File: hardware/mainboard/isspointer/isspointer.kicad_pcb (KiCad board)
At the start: 2 copper layers, 33 parts, among them J1 USB_B_Micro, Q1 SS8050-G, Q2 SS8050-G, SW1 SW_Push, SW2 SW_Push, U1 AMS1117-3.3, U2 CP2102N-A01-GQFN28, U3 esp32-WROOM-32D, U4 DRV8834_HTSSOP

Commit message: stepper drivers
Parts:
- added C10: 10nF/50V(10%), Capacitor_SMD:C_0603_1608Metric_Pad1.05x0.95mm_HandSolder, F.Cu at (102.2, 64.1)
- added C11: 4.7uF/6.3V(10%), Capacitor_SMD:C_0603_1608Metric_Pad1.05x0.95mm_HandSolder, F.Cu at (110.2, 61.6)
- added C12: 100 uF 16V, Capacitor_SMD:CP_Elec_6.3x4.9, F.Cu at (106.0, 71.1)
- added C13: 10uF/10V(20%), Capacitor_SMD:C_0603_1608Metric_Pad1.05x0.95mm_HandSolder, F.Cu at (118.7, 64.1)
- added C14: 0.1uF/50V(10%), Capacitor_SMD:C_0603_1608Metric_Pad1.05x0.95mm_HandSolder, F.Cu at (118.7, 67.3)
- added C15: 0.1uF/50V(10%), Capacitor_SMD:C_0603_1608Metric_Pad1.05x0.95mm_HandSolder, F.Cu at (118.7, 70.5)
- added C16: 10uF/10V(20%), Capacitor_SMD:C_0603_1608Metric_Pad1.05x0.95mm_HandSolder, F.Cu at (118.7, 74.3)
- added C17: 10nF/50V(10%), Capacitor_SMD:C_0603_1608Metric_Pad1.05x0.95mm_HandSolder, F.Cu at (131.4, 61.0)
- added C18: 4.7uF/6.3V(10%), Capacitor_SMD:C_0603_1608Metric_Pad1.05x0.95mm_HandSolder, F.Cu at (127.0, 63.5)
- added C19: 100 uF 16V, Capacitor_SMD:CP_Elec_6.3x4.9, F.Cu at (130.2, 70.5)
- added C20: 10uF/10V(20%), Capacitor_SMD:C_0603_1608Metric_Pad1.05x0.95mm_HandSolder, F.Cu at (141.0, 61.0)
- added C21: 0.1uF/50V(10%), Capacitor_SMD:C_0603_1608Metric_Pad1.05x0.95mm_HandSolder, F.Cu at (140.7, 65.4)
- added C22: 0.1uF/50V(10%), Capacitor_SMD:C_0603_1608Metric_Pad1.05x0.95mm_HandSolder, F.Cu at (141.0, 67.9)
- added C23: 10uF/10V(20%), Capacitor_SMD:C_0603_1608Metric_Pad1.05x0.95mm_HandSolder, F.Cu at (141.0, 71.8)
- added J2: Motor 1, Connector_JST:JST_XH_B5B-XH-A_1x05_P2.50mm_Vertical, F.Cu at (112.2, 35.6)
- added J3: Motor 2, Connector_JST:JST_XH_B5B-XH-A_1x05_P2.50mm_Vertical, F.Cu at (137.7, 34.9)
- added R11: 47K(5%), Resistor_SMD:R_0603_1608Metric_Pad1.05x0.95mm_HandSolder, F.Cu at (107.3, 48.9)
- added R12: 1.5K(5%), Resistor_SMD:R_0603_1608Metric_Pad1.05x0.95mm_HandSolder, F.Cu at (115.0, 69.6)
- added R13: 10K(5%), Resistor_SMD:R_0603_1608Metric_Pad1.05x0.95mm_HandSolder, F.Cu at (112.4, 68.6)
- added R14: 47K(5%), Resistor_SMD:R_0603_1608Metric_Pad1.05x0.95mm_HandSolder, F.Cu at (115.2, 50.2)
- added R15: 47K(5%), Resistor_SMD:R_0603_1608Metric_Pad1.05x0.95mm_HandSolder, F.Cu at (115.6, 54.6)
- added R16: 100(5%) 1W, Resistor_SMD:R_2512_6332Metric_Pad1.52x3.35mm_HandSolder, F.Cu at (101.6, 44.5)
- added R17: 100(5%) 1W, Resistor_SMD:R_2512_6332Metric_Pad1.52x3.35mm_HandSolder, F.Cu at (113.7, 44.5)
- added R18: 1(20%), Resistor_SMD:R_0603_1608Metric_Pad1.05x0.95mm_HandSolder, F.Cu at (115.0, 72.1)
- added R19: 47K(5%), Resistor_SMD:R_0603_1608Metric_Pad1.05x0.95mm_HandSolder, F.Cu at (132.1, 48.3)
- added R20: 1.5K(5%), Resistor_SMD:R_0603_1608Metric_Pad1.05x0.95mm_HandSolder, F.Cu at (132.5, 65.4)
- added R21: 10K(5%), Resistor_SMD:R_0603_1608Metric_Pad1.05x0.95mm_HandSolder, F.Cu at (135.9, 67.9)
- added R22: 47K(5%), Resistor_SMD:R_0603_1608Metric_Pad1.05x0.95mm_HandSolder, F.Cu at (139.1, 49.5)
- added R23: 47K(5%), Resistor_SMD:R_0603_1608Metric_Pad1.05x0.95mm_HandSolder, F.Cu at (139.1, 54.0)
- added R24: 100(5%) 1W, Resistor_SMD:R_2512_6332Metric_Pad1.52x3.35mm_HandSolder, F.Cu at (127.0, 43.8)
- added R25: 100(5%) 1W, Resistor_SMD:R_2512_6332Metric_Pad1.52x3.35mm_HandSolder, F.Cu at (138.4, 43.8)
- added R26: 1(20%), Resistor_SMD:R_0603_1608Metric_Pad1.05x0.95mm_HandSolder, F.Cu at (138.4, 76.8)
- added RV1: R_POT_US, digikey-footprints:Trimpot_3.8mmx3.6mm_TC33X-2-103E, F.Cu at (116.2, 58.4)
- added RV2: R_POT_US, digikey-footprints:Trimpot_3.8mmx3.6mm_TC33X-2-103E, F.Cu at (140.3, 57.8)
- added U5: DRV8834_HTSSOP, isspointer:DRV8834PWPR, F.Cu at (131.4, 55.2)
- moved U4 16.8 mm to (107.3, 55.9), turned to 270 degrees
- moved SW1 2.54 mm to (92.7, 62.2)
- moved C8 1.79 mm to (83.6, 65.5)
- moved C7 1.27 mm to (83.4, 59.4)
- moved C9 1.27 mm to (83.3, 62.7)
- moved SW2 1.27 mm to (73.7, 62.2)
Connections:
- net Net-(U4-Pad11) renamed /STEP_1
- net Net-(U4-Pad12) renamed /DIR_1
- net VDD renamed +3V3
- U4 pad 1: Net-(U4-Pad1) -> /ENABLE_1
- U4 pad 13: Net-(U4-Pad13) -> GNDREF
- U4 pad 14: Net-(U4-Pad14) -> GNDREF
- U4 pad 18: Net-(U4-Pad18) -> VBUS
- U4 pad 19: Net-(U4-Pad19) -> VBUS
- U4 pad 20: Net-(U4-Pad20) -> +5V
- U4 pad 21: Net-(U4-Pad21) -> Net-(RV1-Pad3)
- U4 pad 22: Net-(U4-Pad22) -> Net-(RV1-Pad2)
- U4 pad 23: Net-(U4-Pad23) -> Net-(RV1-Pad2)
- U4 pad 25: Net-(U4-Pad25) -> Net-(RV1-Pad3)
- U4 pad 4: Net-(U4-Pad4) -> /A1_1
- U4 pad 6: Net-(U4-Pad6) -> /A2_1
- U4 pad 7: Net-(U4-Pad7) -> /B2_1
- U4 pad 9: Net-(U4-Pad9) -> /B1_1
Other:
- board text added: "motor 1"
- board text added: "motor 2"

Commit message: endstops and accel circuit board
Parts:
- added C24: 0.22uF/50V(10%), Capacitor_SMD:C_0603_1608Metric_Pad1.05x0.95mm_HandSolder, F.Cu at (113.0, 88.3)
- added C25: 4.7uF/50V(10%), Capacitor_SMD:C_0603_1608Metric_Pad1.05x0.95mm_HandSolder, F.Cu at (113.0, 92.1)
- added Q3: DMN67D8L, Package_TO_SOT_SMD:SOT-23, F.Cu at (108.6, 84.5)
- added Q4: DMN67D8L, Package_TO_SOT_SMD:SOT-23, F.Cu at (110.5, 99.7)
- added R27: 4.7K(5%), Resistor_SMD:R_0603_1608Metric_Pad1.05x0.95mm_HandSolder, F.Cu at (116.2, 92.7)
- added R28: 4.7K(5%), Resistor_SMD:R_0603_1608Metric_Pad1.05x0.95mm_HandSolder, F.Cu at (110.7, 96.1)
- added R29: 4.7K(5%), Resistor_SMD:R_0603_1608Metric_Pad1.05x0.95mm_HandSolder, F.Cu at (113.0, 83.2)
- added R30: 4.7K(5%), Resistor_SMD:R_0603_1608Metric_Pad1.05x0.95mm_HandSolder, F.Cu at (116.2, 88.3)
- added R31: 330(5%), Resistor_SMD:R_0603_1608Metric_Pad1.05x0.95mm_HandSolder, F.Cu at (82.5, 89.5)
- added R32: 4.7K(5%), Resistor_SMD:R_0603_1608Metric_Pad1.05x0.95mm_HandSolder, F.Cu at (86.1, 85.1)
- added R33: 330(5%), Resistor_SMD:R_0603_1608Metric_Pad1.05x0.95mm_HandSolder, F.Cu at (99.7, 89.9)
- added R34: 4.7K(5%), Resistor_SMD:R_0603_1608Metric_Pad1.05x0.95mm_HandSolder, F.Cu at (103.5, 85.7)
- added U6: LSM303DLHC, Package_LGA:LGA-14_3x5mm_P0.8mm_LayoutBorder1x6y, F.Cu at (109.9, 90.2)
- added U7: EE-SX3350, isspointer:EE-SX3350, F.Cu at (87.0, 93.3)
- added U8: EE-SX3350, isspointer:EE-SX3350, F.Cu at (104.1, 94.0)
- C10, C17, C20: footprint Capacitor_SMD:C_0603_1608Metric_Pad1.05x0.95mm_HandSolder -> Capacitor_SMD:C_0402_1005Metric
- C11, C18: value 4.7uF/6.3V(10%) -> 2.2uF/6.3V(10%); footprint Capacitor_SMD:C_0603_1608Metric_Pad1.05x0.95mm_HandSolder -> Capacitor_SMD:C_0402_1005Metric
- C14: value 0.1uF/50V(10%) -> 10nF/50V(10%); footprint Capacitor_SMD:C_0603_1608Metric_Pad1.05x0.95mm_HandSolder -> Capacitor_SMD:C_0402_1005Metric
- C2, C4, C5: footprint Capacitor_SMD:C_0603_1608Metric_Pad1.05x0.95mm_HandSolder -> Capacitor_SMD:C_1206_3216Metric_Pad1.42x1.75mm_HandSolder
- moved C16 35.8 mm to (99.1, 44.5)
- moved R26 34.5 mm to (123.4, 45.7), turned to 180 degrees
- moved C23 33.7 mm to (123.2, 43.2)
- moved R18 30.2 mm to (99.3, 46.4), turned to 180 degrees
- moved R12 21.7 mm to (102.2, 52.1), turned to 90 degrees
- moved R13 16.5 mm to (113.0, 52.1), turned to 270 degrees
- moved R21 15.9 mm to (137.2, 52.1), turned to 270 degrees
- moved R20 14.7 mm to (126.4, 52.1), turned to 90 degrees
- moved R19 14.7 mm to (136.5, 62.2), turned to 90 degrees
- moved C15 14.3 mm to (105.4, 65.4), turned to 180 degrees
- moved R11 14.3 mm to (112.4, 62.2), turned to 90 degrees
- moved C13 13.7 mm to (105.4, 67.3), turned to 180 degrees
- moved C14 13.3 mm to (106.0, 63.5), turned to 180 degrees
- moved C22 11.7 mm to (129.5, 65.4), turned to 180 degrees
- moved R23 11.7 mm to (141.6, 42.5), turned to 90 degrees
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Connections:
- net Net-(R11-Pad2) renamed /CONFIG_1
- net Net-(R12-Pad1) renamed /nFAULT_1
- net Net-(R14-Pad2) renamed /BDECAY_1
- net Net-(R15-Pad1) renamed /ADECAY_1
- net Net-(R16-Pad2) renamed /BISEN_1
- net Net-(R17-Pad1) renamed /AISEN_1
- net Net-(RV1-Pad1) renamed /VREF1
- net Net-(RV1-Pad2) renamed /AVREF1
- R21 pad 2: /ENABLE_2 -> /ENABLE_1
- RV1 pad 3: Net-(RV1-Pad3) -> GNDREF
- RV2 pad 3: Net-(RV2-Pad3) -> GNDREF
- U3 pad 11: /IO26 -> /DIR_1
- U3 pad 12: /IO27 -> /DIR_2
- U3 pad 13: /IO14 -> /ENABLE_1
- U3 pad 4: /IO36 -> /END_1
- U3 pad 5: /IO39 -> /END_2
- U4 pad 11: /STEP_1 -> /IO33
- U4 pad 21: Net-(RV1-Pad3) -> GNDREF
- U4 pad 25: Net-(RV1-Pad3) -> GNDREF
- U5 pad 1: /ENABLE_2 -> /ENABLE_1
- U5 pad 11: /STEP_2 -> /IO25
- U5 pad 21: Net-(RV2-Pad3) -> GNDREF
- U5 pad 25: Net-(RV2-Pad3) -> GNDREF
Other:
- board outline added: 132.7 x 75.6 mm

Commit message: gps
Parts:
- added C26: 2.2uF/10V(10%), Capacitor_SMD:C_0603_1608Metric_Pad1.05x0.95mm_HandSolder, B.Cu at (73.0, 77.5)
- added C27: 2.2uF/16V(10%), Capacitor_SMD:C_0603_1608Metric_Pad1.05x0.95mm_HandSolder, B.Cu at (81.5, 78.1)
- added C28: 2.2uF/10V(10%), Capacitor_SMD:C_0603_1608Metric_Pad1.05x0.95mm_HandSolder, B.Cu at (73.0, 74.9)
- added C29: 2.2uF/10V(10%), Capacitor_SMD:C_0603_1608Metric_Pad1.05x0.95mm_HandSolder, B.Cu at (68.8, 78.1)
- added C30: 10uF/10V(10%), Capacitor_SMD:C_0603_1608Metric_Pad1.05x0.95mm_HandSolder, B.Cu at (85.7, 78.1)
- added C31: 2.2uF/10V(10%), Capacitor_SMD:C_0603_1608Metric_Pad1.05x0.95mm_HandSolder, B.Cu at (69.5, 75.6)
- added R35: 10K(5%), Resistor_SMD:R_0603_1608Metric_Pad1.05x0.95mm_HandSolder, F.Cu at (102.2, 75.6)
- added R36: 10K(5%), Resistor_SMD:R_0603_1608Metric_Pad1.05x0.95mm_HandSolder, F.Cu at (102.2, 80.4)
- added R37: 10K(5%), Resistor_SMD:R_0603_1608Metric_Pad1.05x0.95mm_HandSolder, F.Cu at (102.9, 87.0)
- added R38: 300K(5%), Resistor_SMD:R_0603_1608Metric_Pad1.05x0.95mm_HandSolder, B.Cu at (78.1, 76.8)
- added R39: 10K(5%), Resistor_SMD:R_0603_1608Metric_Pad1.05x0.95mm_HandSolder, B.Cu at (73.0, 73.0)
- added SW3: Up, Button_Switch_THT:SW_TH_Tactile_Omron_B3F-10xx, F.Cu at (92.7, 69.8)
- added SW4: Select, Button_Switch_THT:SW_TH_Tactile_Omron_B3F-10xx, F.Cu at (92.7, 79.4)
- added SW5: Down, Button_Switch_THT:SW_TH_Tactile_Omron_B3F-10xx, F.Cu at (92.7, 88.9)
- added U9: CFAL12864N, isspointer:CFAL12864N_oled, F.Cu at (76.8, 85.7)
- SW1: value SW_Push -> Boot; footprint Button_Switch_SMD:SW_SPST_B3S-1000 -> Button_Switch_SMD:SW_SPST_CK_RS282G05A3
- SW2: value SW_Push -> Reset; footprint Button_Switch_SMD:SW_SPST_B3S-1000 -> Button_Switch_SMD:SW_SPST_CK_RS282G05A3
- moved R32 35.0 mm to (120.7, 79.4)
- moved R31 34.8 mm to (116.8, 83.8)
- moved U7 23.5 mm to (110.5, 92.7)
- moved Q3 16.6 mm to (125.1, 83.2)
- moved Q4 16.6 mm to (127.0, 98.4)
- moved R27 16.6 mm to (132.7, 91.4)
- moved R30 16.6 mm to (132.7, 87.0)
- moved R33 16.6 mm to (116.2, 88.7)
- moved R34 16.6 mm to (120.0, 84.5)
- moved U8 16.6 mm to (120.6, 92.7)
- moved C24 16.6 mm to (129.5, 87.0)
- moved C25 16.6 mm to (129.5, 90.8)
- moved R28 16.6 mm to (127.2, 94.8)
- moved R29 16.6 mm to (129.5, 81.9)
- moved U6 16.6 mm to (126.4, 88.9)
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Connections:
- U3 pad 6: /IO34 -> /BTN_UP
- U3 pad 7: /IO35 -> /BTN_SELECT
- U3 pad 8: /IO32 -> /BTN_DOWN
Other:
- outline, holes or cut-outs redrawn

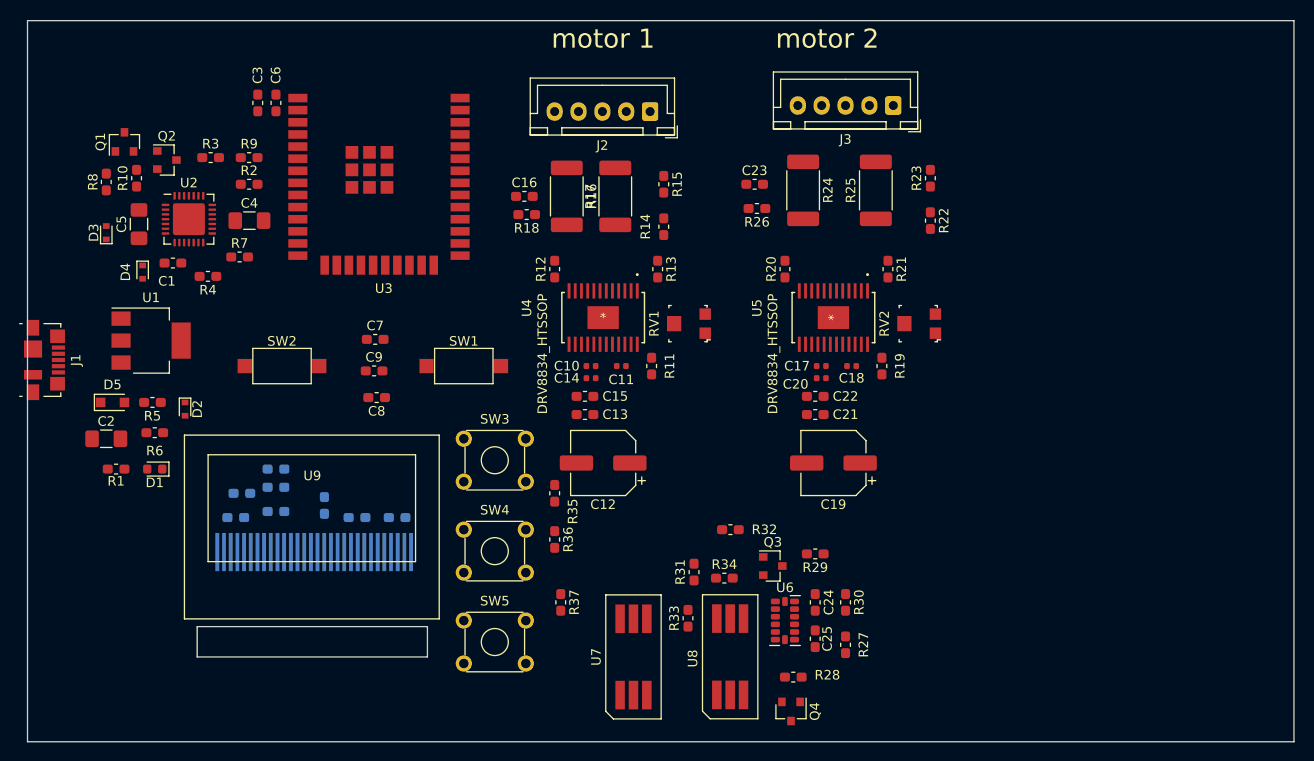
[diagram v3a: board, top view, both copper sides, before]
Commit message: some trace routing
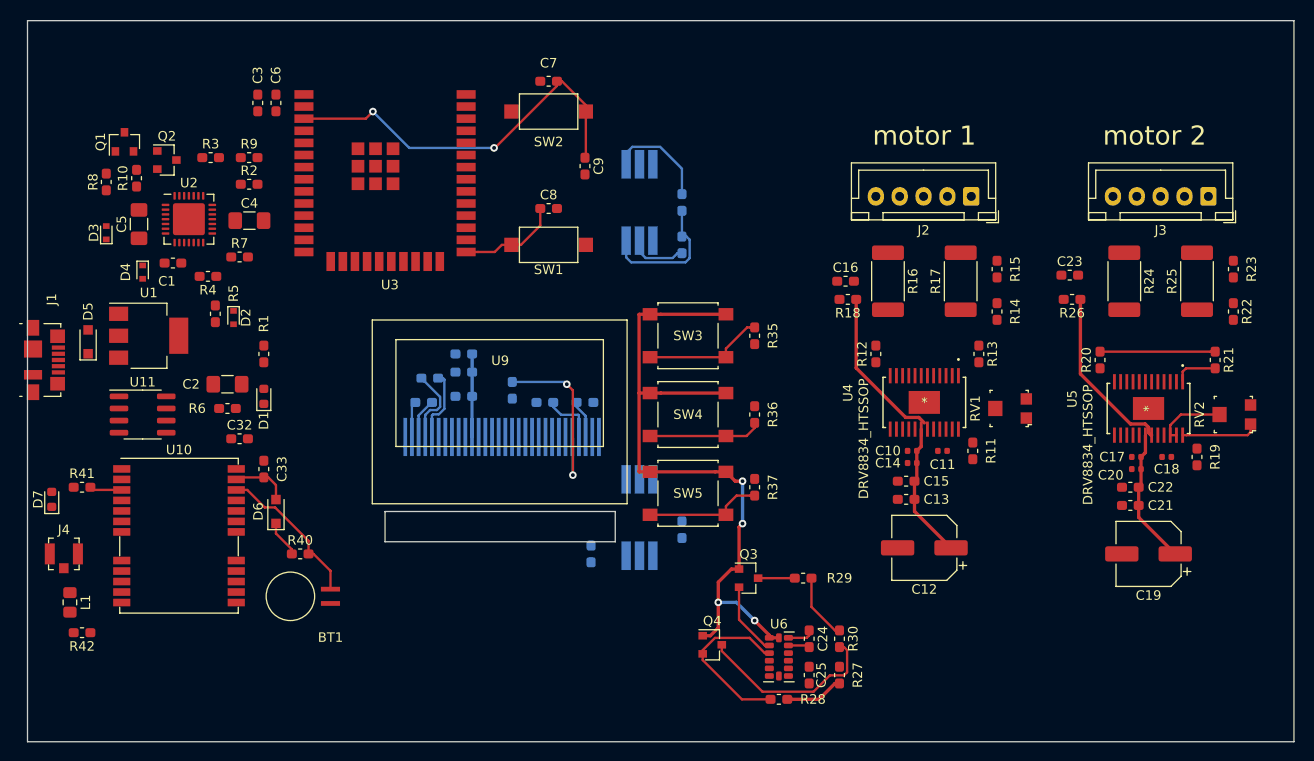
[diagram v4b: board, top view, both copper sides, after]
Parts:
- added BT1: 3V lithium cell, isspointer:MS412FE_FL26E, F.Cu at (78.7, 86.4)
- added C32: 0.1uF/50V(10%), Capacitor_SMD:C_0603_1608Metric_Pad1.05x0.95mm_HandSolder, F.Cu at (69.2, 69.8)
- added C33: 4.7uF, Capacitor_SMD:C_0603_1608Metric_Pad1.05x0.95mm_HandSolder, F.Cu at (71.8, 73.0)
- added D6: D_Schottky, Diode_SMD:D_SOD-323_HandSoldering, F.Cu at (73.0, 77.5)
- added D7: LED, Diode_SMD:D_0603_1608Metric, F.Cu at (49.5, 76.2)
- added J4: U_FL-R-SMT-1_10_, digikey-footprints:Coax_Conn_U.FL, F.Cu at (50.8, 81.9)
- added L1: 27 uH MLF2012C270KT000, Inductor_SMD:L_0805_2012Metric_Pad1.15x1.40mm_HandSolder, F.Cu at (51.4, 87.0)
- added R40: 1K(5%), Resistor_SMD:R_0603_1608Metric_Pad1.05x0.95mm_HandSolder, F.Cu at (75.6, 81.9)
- added R41: 1K(5%), Resistor_SMD:R_0603_1608Metric_Pad1.05x0.95mm_HandSolder, F.Cu at (52.7, 74.9)
- added R42: 22(5%), Resistor_SMD:R_0603_1608Metric_Pad1.05x0.95mm_HandSolder, F.Cu at (52.7, 90.2)
- added U10: NEO-6M-0-001, RF_GPS:ublox_NEO, F.Cu at (62.9, 80.0)
- added U11: 24AA32-OT, Package_SO:SOIC-8_3.9x4.9mm_P1.27mm, F.Cu at (59.1, 67.3)
- R31, R32, R33, R34, U7, U8: moved to B.Cu
- RV1, RV2: value R_POT_US -> 10K TRIMMER
- SW3, SW4, SW5: footprint Button_Switch_THT:SW_TH_Tactile_Omron_B3F-10xx -> Button_Switch_SMD:SW_SPST_B3S-1000
- moved U7 47.6 mm to (111.1, 45.1)
- moved R31 38.8 mm to (115.6, 45.1), turned to 270 degrees
- moved SW2 38.6 mm to (101.6, 35.6)
- moved R17 37.3 mm to (144.8, 53.3)
- moved R14 36.0 mm to (148.6, 56.5)
- moved R15 36.0 mm to (148.6, 52.1), turned to 90 degrees
- moved R21 35.6 mm to (171.4, 61.6)
- moved R24 35.0 mm to (161.9, 53.3)
- moved R25 35.0 mm to (169.5, 53.3)
- moved R11 34.8 mm to (146.1, 71.1)
- moved R18 34.8 mm to (133.0, 55.2)
- moved RV1 34.8 mm to (149.9, 66.7)
- moved C11 34.8 mm to (142.9, 71.1)
- moved U4 34.8 mm to (141.0, 66.0)
- moved C12 34.8 mm to (141.0, 81.3)
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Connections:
- U3 pad 27: /IO16 -> /ESP_RXD1
- U3 pad 28: /IO17 -> /ESP_TXD1
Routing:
- net +3V3: track 0.00 -> 93.8 mm, vias 0 -> 4
- net VBUS: track 0.00 -> 63.6 mm
- net /EN: track 0.00 -> 41.2 mm, vias 0 -> 2
- net +5V: track 0.00 -> 21.3 mm
- net /IO21: track 0.00 -> 19.6 mm
- net Net-(R38-Pad1): track 0.00 -> 19.6 mm, vias 0 -> 2
- net /SDALV: track 0.00 -> 18.0 mm
- net Net-(BT1-Pad1): track 0.00 -> 16.1 mm
- net /BTN_UP: track 0.00 -> 12.8 mm
- net /BTN_DOWN: track 0.00 -> 12.3 mm
- net Net-(R20-Pad2): track 0.00 -> 12.1 mm
- net /BTN_SELECT: track 0.00 -> 11.8 mm
- net Net-(R31-Pad1): track 0.00 -> 10.9 mm
- net /IO0: track 0.00 -> 10.7 mm
- net Net-(RV2-Pad1): track 0.00 -> 8.10 mm
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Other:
- outline, holes or cut-outs redrawn
- net class 5v added: clearance 0.2, trace_width 0.35, via_dia 0.8, via_drill 0.4

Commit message: work MITAI bluetooth connection
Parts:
- added REF**: MountingHole_3.2mm_M3, MountingHole:MountingHole_3.2mm_M3, F.Cu at (51.4, 85.1)
- added REF**: MountingHole_3.2mm_M3, MountingHole:MountingHole_3.2mm_M3, F.Cu at (158.1, 85.1)
- added REF**: MountingHole_3.2mm_M3, MountingHole:MountingHole_3.2mm_M3, F.Cu at (157.5, 31.8)
- added REF**: MountingHole_3.2mm_M3, MountingHole:MountingHole_3.2mm_M3, F.Cu at (51.4, 30.5)
- BT1, C1, C10, C11, C12, C13, C14, C15, C16, C17, C18, C19, C2, C20, C21, C22, C23, C24, C25, C3, C32, C33, C4, C5, C6, C7, C8, C9, D1, D2, D3, D4, D5, D6, D7, J1, J2, J3, J4, L1, Q1, Q2, Q3, Q4, R1, R10, R11, R12, R13, R14, R15, R16, R17, R18, R19, R2, R20, R21, R22, R23, R24, R25, R26, R27, R28, R29, R3, R30, R4, R40, R41, R42, R5, R6, R7, R8, R9, RV1, RV2, SW1, SW2, U1, U10, U11, U2, U3, U4, U5, U6: moved to B.Cu
- moved Q4 65.3 mm to (142.2, 30.5), turned to 180 degrees
- moved U6 58.2 mm to (139.7, 36.2), turned to 180 degrees
- moved Q3 55.8 mm to (136.5, 30.5), turned to 180 degrees
- moved C25 55.0 mm to (142.2, 41.3)
- moved R28 54.4 mm to (139.1, 44.5), turned to 0 degrees
- moved C24 54.3 mm to (136.5, 37.1)
- moved R27 53.5 mm to (135.9, 41.3)
- moved R29 50.4 mm to (142.9, 36.2), turned to 90 degrees
- moved R30 50.0 mm to (139.1, 41.3)
- moved C19 48.6 mm to (149.9, 35.6)
- moved C12 48.2 mm to (125.7, 35.6)
- moved C21 38.4 mm to (148.0, 41.3)
- moved C13 37.0 mm to (125.1, 41.9)
- moved R42 36.1 mm to (73.0, 60.3)
- moved C22 34.9 mm to (148.0, 43.2)
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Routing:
- net +3V3: track 93.8 -> 0.00 mm, vias 4 -> 0
- net VBUS: track 63.6 -> 0.00 mm
- net /EN: track 41.2 -> 0.00 mm, vias 2 -> 0
- net +5V: track 21.3 -> 0.00 mm
- net /IO21: track 19.6 -> 0.00 mm
- net Net-(R38-Pad1): track 19.6 -> 0.00 mm, vias 2 -> 0
- net /SDALV: track 18.0 -> 0.00 mm
- net Net-(BT1-Pad1): track 16.1 -> 0.00 mm
- net /BTN_UP: track 12.8 -> 0.00 mm
- net /BTN_DOWN: track 12.3 -> 0.00 mm
- net Net-(R20-Pad2): track 12.1 -> 0.00 mm
- net /BTN_SELECT: track 11.8 -> 0.00 mm
- net Net-(R31-Pad1): track 10.9 -> 0.00 mm
- net /IO0: track 10.7 -> 0.00 mm
- net Net-(RV2-Pad1): track 8.10 -> 0.00 mm
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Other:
- board size 132.7 x 75.6 mm -> 115.6 x 63.5 mm
